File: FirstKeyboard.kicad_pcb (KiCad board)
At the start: 2 copper layers, 114.3 x 38.1 mm, 33 parts, among them SW1 SW_Push, U1 ATmega32U4-AU, Y1 16MHz

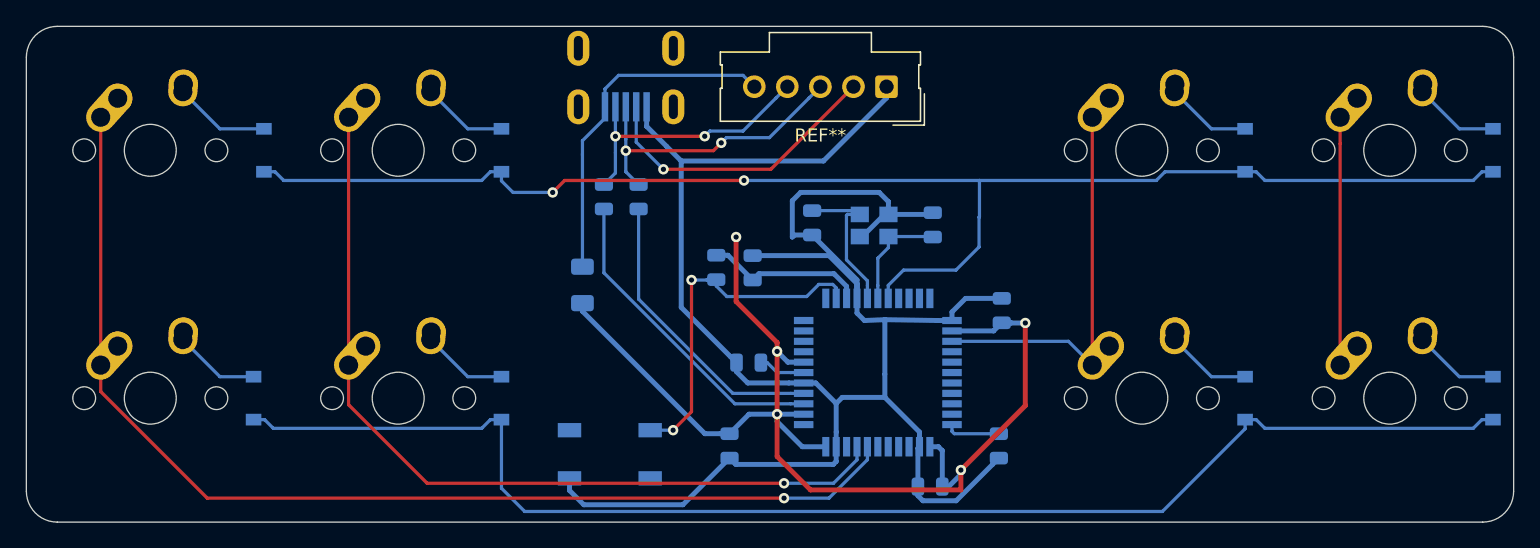
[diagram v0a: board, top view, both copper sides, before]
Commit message: fixed missing traces
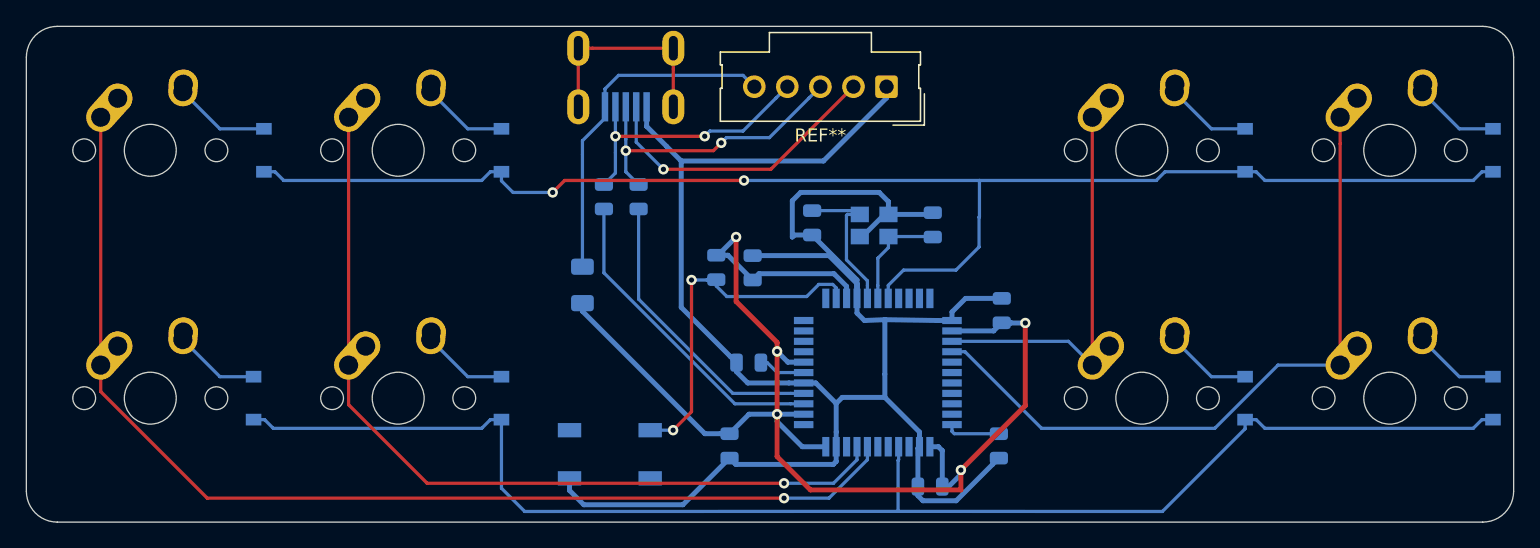
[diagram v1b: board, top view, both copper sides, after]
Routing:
- net Col3: track 19.0 -> 53.3 mm
- net Net-(USB1-Pad6): track 0.00 -> 16.3 mm
- net Row1: track 105.7 -> 110.7 mm
- net +5V: track 102.1 -> 104.2 mm
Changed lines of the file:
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@@
     (thickness 1.6)
     (drawings 8)
-    (tracks 277)
+    (tracks 293)
     (zones 0)
     (modules 33)
@@
     (solder_mask_min_width 0.25)
     (aux_axis_origin 0 0)
-    (visible_elements FFFFFF7F)
+    (visible_elements 7FFFFFFF)
     (pcbplotparams
       (layerselection 0x010fc_ffffffff)
@@
   (segment (start 153.139527 87.271473) (end 158.904625 87.271473) (width 0.381) (layer B.Cu) (net 2))
   (segment (start 152.654 87.757) (end 153.139527 87.271473) (width 0.381) (layer B.Cu) (net 2))
-  (segment (start 149.287 87.727) (end 149.257 87.757) (width 0.381) (layer B.Cu) (net 25))
-  (segment (start 149.987 87.727) (end 149.287 87.727) (width 0.381) (layer B.Cu) (net 25))
   (segment (start 152.375 98.069) (end 154.534 98.069) (width 0.381) (layer B.Cu) (net 2))
   (segment (start 150.876 99.568) (end 152.375 98.069) (width 0.381) (layer B.Cu) (net 2))
@@
   (segment (start 171.17425 91.669) (end 171.79925 91.044) (width 0.381) (layer B.Cu) (net 2))
   (segment (start 167.97425 91.669) (end 171.17425 91.669) (width 0.381) (layer B.Cu) (net 2))
+  (segment (start 149.987 85.852) (end 151.384 84.455) (width 0.381) (layer B.Cu) (net 2))
+  (segment (start 149.86 85.852) (end 149.987 85.852) (width 0.381) (layer B.Cu) (net 2))
   (segment (start 160.5955 82.423) (end 160.8885 82.716) (width 0.25) (layer B.Cu) (net 3))
   (segment (start 157.226 82.423) (end 160.5955 82.423) (width 0.25) (layer B.Cu) (net 3))
@@
   (segment (start 131.831099 99.156401) (end 115.818901 99.156401) (width 0.25) (layer B.Cu) (net 9))
   (segment (start 133.35 98.4875) (end 132.5 98.4875) (width 0.25) (layer B.Cu) (net 9))
-  (segment (start 135.13551 105.54451) (end 184.14299 105.54451) (width 0.25) (layer B.Cu) (net 9))
+  (segment (start 163.83 101.61325) (end 163.83 105.537) (width 0.25) (layer B.Cu) (net 9))
+  (segment (start 135.13551 105.54451) (end 163.83 105.537) (width 0.25) (layer B.Cu) (net 9))
+  (segment (start 163.87425 101.569) (end 163.83 101.61325) (width 0.25) (layer B.Cu) (net 9))
+  (segment (start 163.87425 100.569) (end 163.87425 101.569) (width 0.25) (layer B.Cu) (net 9))
+  (segment (start 163.83 105.537) (end 184.14299 105.54451) (width 0.25) (layer B.Cu) (net 9))
   (segment (start 130.7625 76.1375) (end 133.35 76.1375) (width 0.25) (layer B.Cu) (net 10))
   (segment (start 127.9125 73.2875) (end 130.7625 76.1375) (width 0.25) (layer B.Cu) (net 10))
@@
   (segment (start 197.8025 77.2795) (end 197.8025 94.2975) (width 0.25) (layer F.Cu) (net 20))
   (segment (start 197.8025 75.2475) (end 197.8025 77.2795) (width 0.25) (layer F.Cu) (net 20))
+  (segment (start 168.97425 93.269) (end 167.97425 93.269) (width 0.25) (layer B.Cu) (net 20))
+  (segment (start 188.166101 99.156401) (end 174.861651 99.156401) (width 0.25) (layer B.Cu) (net 20))
+  (segment (start 193.025002 94.2975) (end 188.166101 99.156401) (width 0.25) (layer B.Cu) (net 20))
+  (segment (start 174.861651 99.156401) (end 168.97425 93.269) (width 0.25) (layer B.Cu) (net 20))
+  (segment (start 197.8025 94.2975) (end 193.025002 94.2975) (width 0.25) (layer B.Cu) (net 20))
   (segment (start 142.90675 79.43675) (end 143.891 80.421) (width 0.25) (layer B.Cu) (net 21))
   (segment (start 142.90675 74.44525) (end 142.90675 76.93025) (width 0.25) (layer B.Cu) (net 21))
@@
   (segment (start 155.57425 97.269) (end 156.57425 97.269) (width 0.25) (layer B.Cu) (net 24))
   (segment (start 141.224 82.296) (end 141.224 87.20076) (width 0.25) (layer B.Cu) (net 24))
+  (segment (start 149.287 87.727) (end 149.257 87.757) (width 0.381) (layer B.Cu) (net 25))
+  (segment (start 149.987 87.727) (end 149.287 87.727) (width 0.381) (layer B.Cu) (net 25))
   (segment (start 144.78 99.297) (end 146.541 99.297) (width 0.25) (layer B.Cu) (net 25))
   (segment (start 146.541 99.297) (end 146.541 99.297) (width 0.25) (layer B.Cu) (net 25))
@@
   (segment (start 168.14825 99.568) (end 167.97425 99.394) (width 0.25) (layer B.Cu) (net 26))
   (segment (start 171.577 99.568) (end 168.14825 99.568) (width 0.25) (layer B.Cu) (net 26))
+  (segment (start 139.25675 74.44525) (end 139.25675 69.94525) (width 0.25) (layer F.Cu) (net 47))
+  (segment (start 140.35675 69.94525) (end 146.55675 69.94525) (width 0.25) (layer F.Cu) (net 47))
+  (segment (start 139.25675 69.94525) (end 140.35675 69.94525) (width 0.25) (layer F.Cu) (net 47))
+  (segment (start 146.55675 71.54525) (end 146.55675 74.44525) (width 0.25) (layer F.Cu) (net 47))
+  (segment (start 146.55675 69.94525) (end 146.55675 71.54525) (width 0.25) (layer F.Cu) (net 47))
   (via (at 145.796 79.248) (size 0.8) (drill 0.4) (layers F.Cu B.Cu) (net 48))
   (segment (start 143.70675 74.44525) (end 143.70675 77.15875) (width 0.25) (layer B.Cu) (net 48))
